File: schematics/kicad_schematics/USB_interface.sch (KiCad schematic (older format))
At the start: 13 parts, among them Q1 NPN, Q2 NPN, U8 USB-TYPEB, U9 USBLC6-2P6

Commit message: added modules do-124ab package
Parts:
- removed Q1, Q2: NPN, -SOT23, symbol NPN
- added Q1, Q2: NPN-SC-59, symbol NPN-SC-59
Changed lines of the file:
@@
-EESchema Schematic File Version 2  date Sun 14 Mar 2010 01:29:31 PM EDT
+EESchema Schematic File Version 2  date Sun 14 Mar 2010 02:53:54 PM EDT
 LIBS:power
 LIBS:device
@@
 Comment4 ""
 $EndDescr
+$Comp
+L NPN-SC-59 Q2
+U 1 1 4B9D3096
+P 5100 4750
+F 0 "Q2" H 5100 4600 50  0000 R CNN
+F 1 "NPN-SC-59" H 5100 4900 50  0000 R CNN
+	1    5100 4750
+	0    -1   -1   0
+$EndComp
+$Comp
+L NPN-SC-59 Q1
+U 1 1 4B9D3085
+P 4750 4050
+F 0 "Q1" H 4750 3900 50  0000 R CNN
+F 1 "NPN-SC-59" H 4750 4200 50  0000 R CNN
+	1    4750 4050
+	0    -1   -1   0
+$EndComp
 Connection ~ 3750 4250
 Wire Wire Line
@@
 $EndComp
 $Comp
-L NPN Q2
-U 1 1 4B7E94E8
-P 5100 4750
-F 0 "Q2" H 5250 4750 50  0000 C CNN
-F 1 "NPN" H 5002 4900 50  0000 C CNN
-F 2 "-SOT23" H 5100 4750 60  0001 C CNN
-F 4 "BC847_BC547" H 5100 4750 60  0001 C CNN "Part"
-	1    5100 4750
-	0    -1   -1   0
-$EndComp
-$Comp
 L GND #PWR058
 U 1 1 4B7E94D3
@@
 $EndComp
 $Comp
-L NPN Q1
-U 1 1 4B7E94BC
-P 4750 4050
-F 0 "Q1" H 4900 4050 50  0000 C CNN
-F 1 "NPN" H 4652 4200 50  0000 C CNN
-F 2 "-SOT23" H 4750 4050 60  0001 C CNN
-F 4 "BC847_BC547" H 4750 4050 60  0001 C CNN "Part"
-	1    4750 4050
-	0    -1   -1   0
-$EndComp
-$Comp

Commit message: made some usb changes
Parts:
- removed U8: USB-TYPEB, mini-usb-b, symbol USB-TYPEB
- added U8: USB-MINI-B-SHELL, symbol USB-MINI-B-SHELL
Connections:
- no-connect marks 0 -> 1
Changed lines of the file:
@@
-EESchema Schematic File Version 2  date Sun 14 Mar 2010 02:53:54 PM EDT
+EESchema Schematic File Version 2  date Sun 14 Mar 2010 03:28:34 PM EDT
 LIBS:power
 LIBS:device
@@
 Comment4 ""
 $EndDescr
+NoConn ~ 3500 3350
+Wire Wire Line
+	3900 3500 3900 4250
+Wire Wire Line
+	3900 3500 3500 3500
+Connection ~ 3750 4250
+Wire Wire Line
+	3900 4250 3500 4250
+Wire Wire Line
+	5950 4500 5950 4350
+Wire Wire Line
+	6600 5100 5100 5100
+Wire Wire Line
+	5100 5100 5100 4950
+Wire Wire Line
+	5300 4650 5500 4650
+Wire Wire Line
+	5500 4800 5500 4400
+Wire Wire Line
+	5500 4400 5400 4400
+Wire Wire Line
+	4650 4400 4900 4400
+Wire Wire Line
+	4100 3950 4550 3950
+Connection ~ 5850 3350
+Wire Wire Line
+	5850 3350 5850 3950
+Wire Wire Line
+	5850 3950 5550 3950
+Connection ~ 5850 2450
+Wire Wire Line
+	6150 2450 5850 2450
+Wire Wire Line
+	7450 3050 6750 3050
+Wire Wire Line
+	6250 3050 5650 3050
+Wire Wire Line
+	5650 3200 5850 3200
+Wire Wire Line
+	4450 3350 4050 3350
+Wire Wire Line
+	4050 3350 4050 3200
+Wire Wire Line
+	4050 3200 3500 3200
+Wire Wire Line
+	4450 3200 4200 3200
+Wire Wire Line
+	3500 4250 3500 4150
+Wire Wire Line
+	3750 4250 3750 4200
+Wire Wire Line
+	3750 3650 3500 3650
+Wire Wire Line
+	3750 3650 3750 3700
+Connection ~ 3500 3650
+Wire Wire Line
+	4450 3050 3500 3050
+Wire Wire Line
+	3500 2900 3700 2900
+Wire Wire Line
+	3700 2900 3700 2850
+Wire Wire Line
+	6250 3350 5650 3350
+Wire Wire Line
+	6750 3350 7450 3350
+Wire Wire Line
+	6150 2850 6150 2950
+Wire Wire Line
+	5850 3200 5850 2400
+Wire Wire Line
+	5050 3950 4950 3950
+Wire Wire Line
+	4100 4300 4100 4400
+Wire Wire Line
+	4100 4400 4150 4400
+Wire Wire Line
+	4750 4250 4750 4650
+Wire Wire Line
+	4750 4650 4900 4650
+Connection ~ 5500 4650
+Wire Wire Line
+	5950 5000 5950 5100
+Connection ~ 5950 5100
+Wire Wire Line
+	3300 2550 3550 2550
+Wire Wire Line
+	3550 2550 3550 2900
+Connection ~ 3550 2900
+Wire Wire Line
+	3650 4250 3650 4350
+Wire Wire Line
+	3500 3650 3500 3750
+$Comp
+L USB-MINI-B-SHELL U8
+U 1 1 4B9D385E
+P 3100 3200
+F 0 "U8" H 3050 3650 60  0000 C CNN
+F 1 "USB-MINI-B-SHELL" H 3250 2600 60  0000 C CNN
+	1    3100 3200
+	-1   0    0    -1
+$EndComp
 $Comp
 L NPN-SC-59 Q2
@@
 	0    -1   -1   0
 $EndComp
-Connection ~ 3750 4250
-Wire Wire Line
-	3900 4250 3500 4250
-Wire Wire Line
-	3900 4250 3900 3350
-Wire Wire Line
-	3900 3350 3500 3350
-Wire Wire Line
-	5950 4500 5950 4350
-Wire Wire Line
-	6600 5100 5100 5100
-Wire Wire Line
-	5100 5100 5100 4950
-Wire Wire Line
-	5300 4650 5500 4650
-Wire Wire Line
-	5500 4800 5500 4400
-Wire Wire Line
-	5500 4400 5400 4400
-Wire Wire Line
-	4650 4400 4900 4400
-Wire Wire Line
-	4100 3950 4550 3950
-Connection ~ 5850 3350
-Wire Wire Line
-	5850 3350 5850 3950
-Wire Wire Line
-	5850 3950 5550 3950
-Connection ~ 5850 2450
-Wire Wire Line
-	6150 2450 5850 2450
-Wire Wire Line
-	7450 3050 6750 3050
-Wire Wire Line
-	6250 3050 5650 3050
-Wire Wire Line
-	5650 3200 5850 3200
-Wire Wire Line
-	4450 3350 4050 3350
-Wire Wire Line
-	4050 3350 4050 3200
-Wire Wire Line
-	4050 3200 3500 3200
-Wire Wire Line
-	4450 3200 4200 3200
-Wire Wire Line
-	3500 3500 3500 3750
-Wire Wire Line
-	3500 4250 3500 4150
-Wire Wire Line
-	3750 4250 3750 4200
-Wire Wire Line
-	3500 3650 3750 3650
-Wire Wire Line
-	3750 3650 3750 3700
-Connection ~ 3500 3650
-Wire Wire Line
-	4450 3050 3500 3050
-Wire Wire Line
-	3500 2900 3700 2900
-Wire Wire Line
-	3700 2900 3700 2850
-Wire Wire Line
-	6250 3350 5650 3350
-Wire Wire Line
-	6750 3350 7450 3350
-Wire Wire Line
-	6150 2850 6150 2950
-Wire Wire Line
-	5850 3200 5850 2400
-Wire Wire Line
-	5050 3950 4950 3950
-Wire Wire Line
-	4100 4300 4100 4400
-Wire Wire Line
-	4100 4400 4150 4400
-Wire Wire Line
-	4750 4250 4750 4650
-Wire Wire Line
-	4750 4650 4900 4650
-Connection ~ 5500 4650
-Wire Wire Line
-	5950 5000 5950 5100
-Connection ~ 5950 5100
-Wire Wire Line
-	3300 2550 3550 2550
-Wire Wire Line
-	3550 2550 3550 2900
-Connection ~ 3550 2900
-Wire Wire Line
-	3650 4250 3650 4350
 $Comp
 L GND #PWR056
@@
 	1    0    0    -1
 $EndComp
-$Comp
-L USB-TYPEB U8
-U 1 1 4B7E9254
-P 3100 3200
-F 0 "U8" H 3050 3650 60  0000 C CNN
-F 1 "USB-TYPEB" H 3300 2600 60  0000 C CNN
-F 2 "mini-usb-b" H 3100 3200 60  0001 C CNN
-	1    3100 3200
-	-1   0    0    -1
-$EndComp
 $EndSCHEMATC

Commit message: modified pinout on em406, update schematic, and modified pinout on S08 and SSOT6
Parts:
- Q1, Q2: footprint (none) -> -SOT23
- U8: footprint (none) -> mini-usb-b-shell
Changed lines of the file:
@@
-EESchema Schematic File Version 2  date Sun 14 Mar 2010 03:28:34 PM EDT
+EESchema Schematic File Version 2  date Sun 14 Mar 2010 03:55:01 PM EDT
 LIBS:power
 LIBS:device
@@
 F 0 "U8" H 3050 3650 60  0000 C CNN
 F 1 "USB-MINI-B-SHELL" H 3250 2600 60  0000 C CNN
+F 2 "mini-usb-b-shell" H 3100 3200 60  0001 C CNN
 	1    3100 3200
 	-1   0    0    -1
@@
 F 0 "Q2" H 5100 4600 50  0000 R CNN
 F 1 "NPN-SC-59" H 5100 4900 50  0000 R CNN
+F 2 "-SOT23" H 5100 4750 60  0001 C CNN
 	1    5100 4750
 	0    -1   -1   0
@@
 F 0 "Q1" H 4750 3900 50  0000 R CNN
 F 1 "NPN-SC-59" H 4750 4200 50  0000 R CNN
+F 2 "-SOT23" H 4750 4050 60  0001 C CNN
 	1    4750 4050
 	0    -1   -1   0
 $EndComp
 $Comp
-L GND #PWR056
+L GND #PWR055
 U 1 1 4B9843F1
 P 3650 4350
-F 0 "#PWR056" H 3650 4350 30  0001 C CNN
+F 0 "#PWR055" H 3650 4350 30  0001 C CNN
 F 1 "GND" H 3650 4280 30  0001 C CNN
 	1    3650 4350
@@
 $EndComp
 $Comp
-L 3V3 #PWR057
+L 3V3 #PWR056
 U 1 1 4B7E9511
 P 4100 4300
-F 0 "#PWR057" H 4100 4400 40  0001 C CNN
+F 0 "#PWR056" H 4100 4400 40  0001 C CNN
 F 1 "U5V" H 4100 4449 40  0000 C CNN
 	1    4100 4300
@@
 $EndComp
 $Comp
-L GND #PWR058
+L GND #PWR057
 U 1 1 4B7E94D3
 P 6150 2950
-F 0 "#PWR058" H 6150 2950 30  0001 C CNN
+F 0 "#PWR057" H 6150 2950 30  0001 C CNN
 F 1 "GND" H 6150 2880 30  0001 C CNN
 	1    6150 2950
@@
 $EndComp
 $Comp
-L 3V3 #PWR059
+L 3V3 #PWR058
 U 1 1 4B7E945B
 P 5850 2400
-F 0 "#PWR059" H 5850 2500 40  0001 C CNN
+F 0 "#PWR058" H 5850 2500 40  0001 C CNN
 F 1 "U5V" H 5850 2549 40  0000 C CNN
 	1    5850 2400
@@
 $EndComp
 $Comp
-L GND #PWR060
+L GND #PWR059
 U 1 1 4B7E9432
 P 5500 4800
-F 0 "#PWR060" H 5500 4800 30  0001 C CNN
+F 0 "#PWR059" H 5500 4800 30  0001 C CNN
 F 1 "GND" H 5500 4730 30  0001 C CNN
 	1    5500 4800
@@
 $EndComp
 $Comp
-L 3V3 #PWR061
+L 3V3 #PWR060
 U 1 1 4B7E93C0
 P 3700 2850
-F 0 "#PWR061" H 3700 2950 40  0001 C CNN
+F 0 "#PWR060" H 3700 2950 40  0001 C CNN
 F 1 "U5V" H 3700 2999 40  0000 C CNN
 	1    3700 2850
@@
 $EndComp
 $Comp
-L GND #PWR062
+L GND #PWR061
 U 1 1 4B7E92CC
 P 4200 3200
-F 0 "#PWR062" H 4200 3200 30  0001 C CNN
+F 0 "#PWR061" H 4200 3200 30  0001 C CNN
 F 1 "GND" H 4200 3130 30  0001 C CNN
 	1    4200 3200

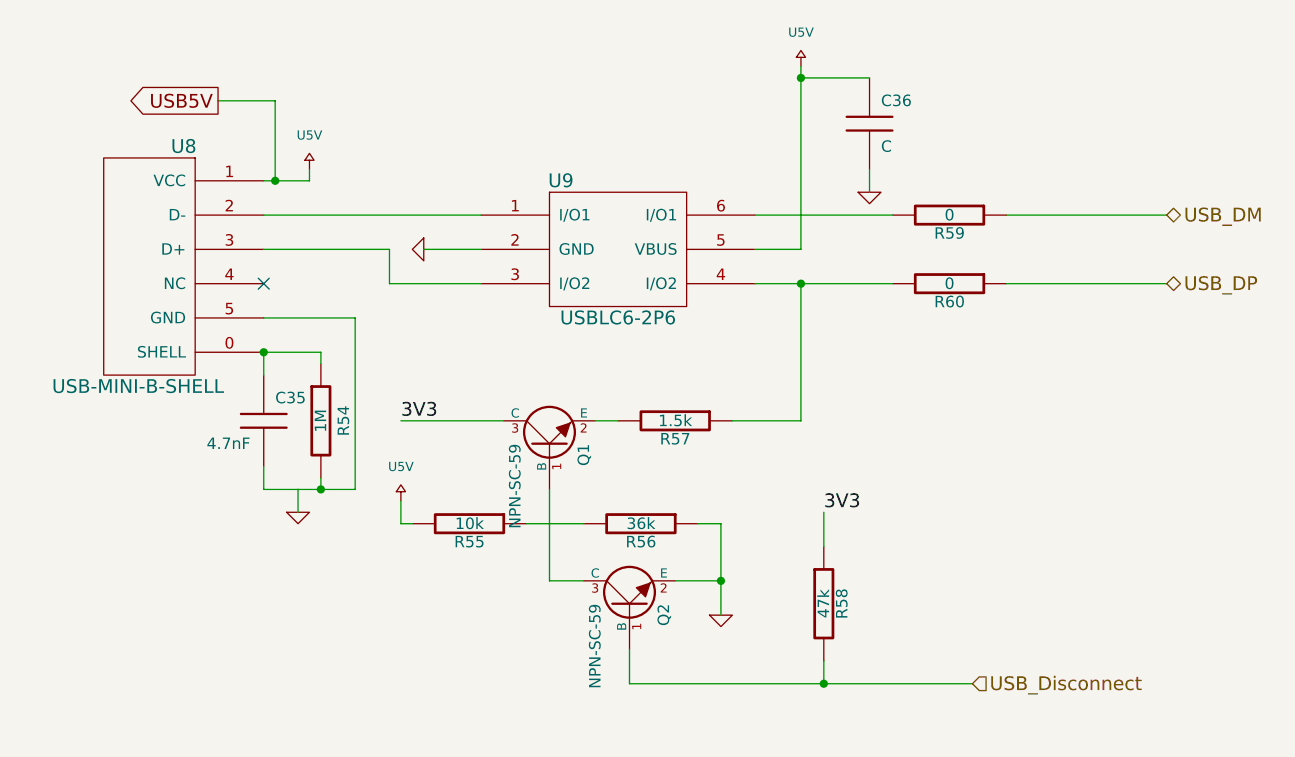
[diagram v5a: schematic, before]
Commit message: Modified power libraries. Now using custom power.lib. This is important Removed outdated crystal libaries Changed some caps to 0603 mounts started PCB layout
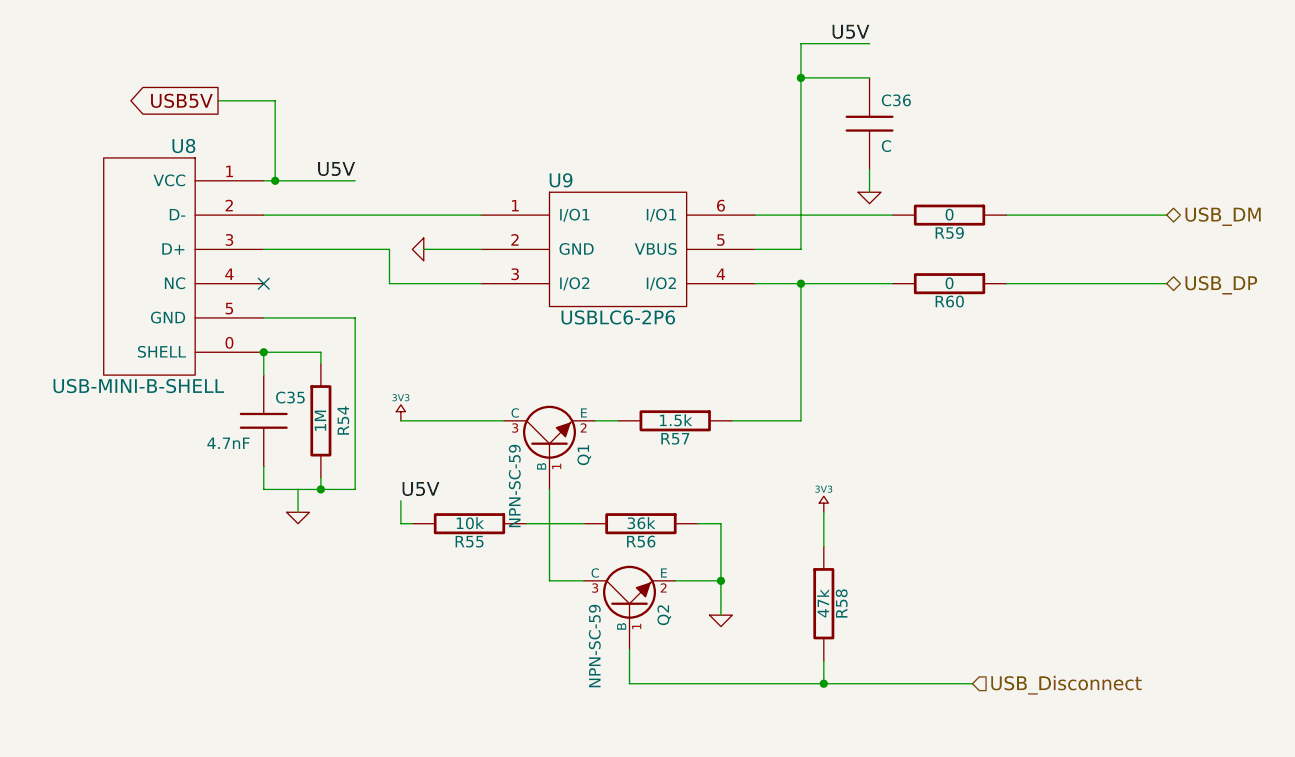
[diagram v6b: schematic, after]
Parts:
- C35, C36, R54, R55, R56, R57, R58, R59, R60: footprint SM0805 -> SM0805-CUSTOM
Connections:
- net 3V3: no longer C36.1, R55.2, U8.1 (VCC), U9.5 (VBUS)
- new net USB5V: C36.1, R55.2, U8.1 (VCC), U9.5 (VBUS)
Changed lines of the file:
@@
-EESchema Schematic File Version 2  date Mon 15 Mar 2010 09:49:52 PM EDT
+EESchema Schematic File Version 2  date Tue 16 Mar 2010 05:07:11 PM EDT
 LIBS:power
 LIBS:device
@@
 Comment4 ""
 $EndDescr
+$Comp
+L GND #PWR073
+U 1 1 4B9FDA7B
+P 4200 3200
+F 0 "#PWR073" H 4200 3200 30  0001 C CNN
+F 1 "GND" H 4200 3130 30  0001 C CNN
+	1    4200 3200
+	0    1    1    0
+$EndComp
+$Comp
+L GND #PWR074
+U 1 1 4B9FDA6F
+P 6150 2950
+F 0 "#PWR074" H 6150 2950 30  0001 C CNN
+F 1 "GND" H 6150 2880 30  0001 C CNN
+	1    6150 2950
+	1    0    0    -1
+$EndComp
+$Comp
+L 3V3 #PWR075
+U 1 1 4B9FDA6B
+P 5950 4350
+F 0 "#PWR075" H 5950 4480 20  0001 C CNN
+F 1 "3V3" H 5950 4450 30  0000 C CNN
+	1    5950 4350
+	1    0    0    -1
+$EndComp
+$Comp
+L GND #PWR076
+U 1 1 4B9FDA67
+P 5500 4800
+F 0 "#PWR076" H 5500 4800 30  0001 C CNN
+F 1 "GND" H 5500 4730 30  0001 C CNN
+	1    5500 4800
+	1    0    0    -1
+$EndComp
+$Comp
+L 3V3 #PWR077
+U 1 1 4B9FDA63
+P 4100 3950
+F 0 "#PWR077" H 4100 4080 20  0001 C CNN
+F 1 "3V3" H 4100 4050 30  0000 C CNN
+	1    4100 3950
+	1    0    0    -1
+$EndComp
+$Comp
+L GND #PWR078
+U 1 1 4B9FDA5F
+P 3650 4350
+F 0 "#PWR078" H 3650 4350 30  0001 C CNN
+F 1 "GND" H 3650 4280 30  0001 C CNN
+	1    3650 4350
+	1    0    0    -1
+$EndComp
+Text Label 4100 4300 0    60   ~ 0
+U5V
+Text Label 6150 2300 2    60   ~ 0
+U5V
+Connection ~ 5850 2450
+Wire Wire Line
+	6150 2300 5850 2300
+Wire Wire Line
+	5850 2300 5850 3200
+Wire Wire Line
+	3500 3750 3500 3650
+Wire Wire Line
+	3650 4250 3650 4350
+Connection ~ 3550 2900
+Wire Wire Line
+	3550 2900 3550 2550
+Wire Wire Line
+	3550 2550 3300 2550
+Connection ~ 5950 5100
+Wire Wire Line
+	5950 5000 5950 5100
+Connection ~ 5500 4650
+Wire Wire Line
+	4900 4650 4750 4650
+Wire Wire Line
+	4750 4650 4750 4250
+Wire Wire Line
+	4150 4400 4100 4400
+Wire Wire Line
+	4100 4400 4100 4300
+Wire Wire Line
+	5050 3950 4950 3950
+Wire Wire Line
+	6150 2850 6150 2950
+Wire Wire Line
+	6750 3350 7450 3350
+Wire Wire Line
+	5650 3350 6250 3350
+Wire Wire Line
+	3900 2900 3500 2900
+Wire Wire Line
+	4450 3050 3500 3050
+Connection ~ 3500 3650
+Wire Wire Line
+	3750 3700 3750 3650
+Wire Wire Line
+	3750 3650 3500 3650
+Wire Wire Line
+	3750 4200 3750 4250
+Wire Wire Line
+	3500 4150 3500 4250
+Wire Wire Line
+	4450 3200 4200 3200
+Wire Wire Line
+	3500 3200 4050 3200
+Wire Wire Line
+	4050 3200 4050 3350
+Wire Wire Line
+	4050 3350 4450 3350
+Wire Wire Line
+	5850 3200 5650 3200
+Wire Wire Line
+	6250 3050 5650 3050
+Wire Wire Line
+	7450 3050 6750 3050
+Wire Wire Line
+	5850 2450 6150 2450
+Wire Wire Line
+	5550 3950 5850 3950
+Wire Wire Line
+	5850 3950 5850 3350
+Connection ~ 5850 3350
+Wire Wire Line
+	4100 3950 4550 3950
+Wire Wire Line
+	4650 4400 4900 4400
+Wire Wire Line
+	5400 4400 5500 4400
+Wire Wire Line
+	5500 4400 5500 4800
+Wire Wire Line
+	5300 4650 5500 4650
+Wire Wire Line
+	5100 4950 5100 5100
+Wire Wire Line
+	5100 5100 6600 5100
+Wire Wire Line
+	5950 4500 5950 4350
+Wire Wire Line
+	3500 4250 3900 4250
+Connection ~ 3750 4250
+Wire Wire Line
+	3500 3500 3900 3500
+Wire Wire Line
+	3900 3500 3900 4250
+Text Label 3900 2900 2    60   ~ 0
+U5V
 NoConn ~ 3500 3350
-Wire Wire Line
-	3900 3500 3900 4250
-Wire Wire Line
-	3900 3500 3500 3500
-Connection ~ 3750 4250
-Wire Wire Line
-	3900 4250 3500 4250
-Wire Wire Line
-	5950 4500 5950 4350
-Wire Wire Line
-	6600 5100 5100 5100
-Wire Wire Line
-	5100 5100 5100 4950
-Wire Wire Line
-	5300 4650 5500 4650
-Wire Wire Line
-	5500 4800 5500 4400
-Wire Wire Line
-	5500 4400 5400 4400
-Wire Wire Line
-	4650 4400 4900 4400
-Wire Wire Line
-	4100 3950 4550 3950
-Connection ~ 5850 3350
-Wire Wire Line
-	5850 3350 5850 3950
-Wire Wire Line
-	5850 3950 5550 3950
-Connection ~ 5850 2450
-Wire Wire Line
-	6150 2450 5850 2450
-Wire Wire Line
-	7450 3050 6750 3050
-Wire Wire Line
-	6250 3050 5650 3050
-Wire Wire Line
-	5650 3200 5850 3200
-Wire Wire Line
-	4450 3350 4050 3350
-Wire Wire Line
-	4050 3350 4050 3200
-Wire Wire Line
-	4050 3200 3500 3200
-Wire Wire Line
-	4450 3200 4200 3200
-Wire Wire Line
-	3500 4250 3500 4150
-Wire Wire Line
-	3750 4250 3750 4200
-Wire Wire Line
-	3750 3650 3500 3650
-Wire Wire Line
-	3750 3650 3750 3700
-Connection ~ 3500 3650
-Wire Wire Line
-	4450 3050 3500 3050
-Wire Wire Line
-	3500 2900 3700 2900
-Wire Wire Line
-	3700 2900 3700 2850
-Wire Wire Line
-	6250 3350 5650 3350
-Wire Wire Line
-	6750 3350 7450 3350
-Wire Wire Line
-	6150 2850 6150 2950
-Wire Wire Line
-	5850 3200 5850 2400
-Wire Wire Line
-	5050 3950 4950 3950
-Wire Wire Line
-	4100 4300 4100 4400
-Wire Wire Line
-	4100 4400 4150 4400
-Wire Wire Line
-	4750 4250 4750 4650
-Wire Wire Line
-	4750 4650 4900 4650
-Connection ~ 5500 4650
-Wire Wire Line
-	5950 5000 5950 5100
-Connection ~ 5950 5100
-Wire Wire Line
-	3300 2550 3550 2550
-Wire Wire Line
-	3550 2550 3550 2900
-Connection ~ 3550 2900
-Wire Wire Line
-	3650 4250 3650 4350
-Wire Wire Line
-	3500 3650 3500 3750
 $Comp
 L USB-MINI-B-SHELL U8
@@
 	0    -1   -1   0
 $EndComp
-$Comp
-L GND #PWR67
-U 1 1 4B9843F1
-P 3650 4350
-F 0 "#PWR67" H 3650 4350 30  0001 C CNN
-F 1 "GND" H 3650 4280 30  0001 C CNN
-	1    3650 4350
-	1    0    0    -1
-$EndComp
 Text GLabel 3300 2550 0    60   Output ~ 0
 USB5V
@@
 Text HLabel 6600 5100 2    60   Input ~ 0
 USB_Disconnect
-Text Label 5950 4350 0    60   ~ 0
-3V3
-Text Label 4100 3950 0    60   ~ 0
-3V3
 $Comp
 L R R58
@@
 F 0 "R58" V 6030 4750 50  0000 C CNN
 F 1 "47k" V 5950 4750 50  0000 C CNN
-F 2 "SM0805" H 5950 4750 60  0001 C CNN
+F 2 "SM0805-CUSTOM" H 5950 4750 60  0001 C CNN
 	1    5950 4750
 	1    0    0    -1
@@
 F 0 "R55" V 4480 4400 50  0000 C CNN
 F 1 "10k" V 4400 4400 50  0000 C CNN
-F 2 "SM0805" H 4400 4400 60  0001 C CNN
+F 2 "SM0805-CUSTOM" H 4400 4400 60  0001 C CNN
 	1    4400 4400
 	0    1    1    0
@@
 F 0 "R56" V 5230 4400 50  0000 C CNN
 F 1 "36k" V 5150 4400 50  0000 C CNN
-F 2 "SM0805" H 5150 4400 60  0001 C CNN
+F 2 "SM0805-CUSTOM" H 5150 4400 60  0001 C CNN
 	1    5150 4400
 	0    1    1    0
@@
 F 0 "R57" V 5380 3950 50  0000 C CNN
 F 1 "1.5k" V 5300 3950 50  0000 C CNN
-F 2 "SM0805" H 5300 3950 60  0001 C CNN
+F 2 "SM0805-CUSTOM" H 5300 3950 60  0001 C CNN
 	1    5300 3950
 	0    1    1    0
-$EndComp
-$Comp
-L 3V3 #PWR69
-U 1 1 4B7E9511
-P 4100 4300
-F 0 "#PWR69" H 4100 4400 40  0001 C CNN
-F 1 "U5V" H 4100 4449 40  0000 C CNN
-	1    4100 4300
-	1    0    0    -1
-$EndComp
-$Comp
-L GND #PWR73
-U 1 1 4B7E94D3
-P 6150 2950
-F 0 "#PWR73" H 6150 2950 30  0001 C CNN
-F 1 "GND" H 6150 2880 30  0001 C CNN
-	1    6150 2950
-	1    0    0    -1
 $EndComp
 $Comp
@@
 F 0 "C36" H 6200 2750 50  0000 L CNN
 F 1 "C" H 6200 2550 50  0000 L CNN
-F 2 "SM0805" H 6150 2650 60  0001 C CNN
+F 2 "SM0805-CUSTOM" H 6150 2650 60  0001 C CNN
 	1    6150 2650
 	1    0    0    -1
@@
 F 0 "R60" V 6580 3350 50  0000 C CNN
 F 1 "0" V 6500 3350 50  0000 C CNN
-F 2 "SM0805" H 6500 3350 60  0001 C CNN
+F 2 "SM0805-CUSTOM" H 6500 3350 60  0001 C CNN
 	1    6500 3350
 	0    1    1    0
@@
 F 0 "R59" V 6580 3050 50  0000 C CNN
 F 1 "0" V 6500 3050 50  0000 C CNN
-F 2 "SM0805" H 6500 3050 60  0001 C CNN
+F 2 "SM0805-CUSTOM" H 6500 3050 60  0001 C CNN
 	1    6500 3050
 	0    1    1    0
-$EndComp
-$Comp
-L 3V3 #PWR72
-U 1 1 4B7E945B
-P 5850 2400
-F 0 "#PWR72" H 5850 2500 40  0001 C CNN
-F 1 "U5V" H 5850 2549 40  0000 C CNN
-	1    5850 2400
-	1    0    0    -1
-$EndComp
-$Comp
-L GND #PWR71
-U 1 1 4B7E9432
-P 5500 4800
-F 0 "#PWR71" H 5500 4800 30  0001 C CNN
-F 1 "GND" H 5500 4730 30  0001 C CNN
-	1    5500 4800
-	1    0    0    -1
 $EndComp
 $Comp
@@
 F 0 "R54" V 3850 3950 50  0000 C CNN
 F 1 "1M" V 3750 3950 50  0000 C CNN
-F 2 "SM0805" H 3750 3950 60  0001 C CNN
+F 2 "SM0805-CUSTOM" H 3750 3950 60  0001 C CNN
 	1    3750 3950
 	1    0    0    -1
@@
 F 0 "C35" H 3550 4050 50  0000 L CNN
 F 1 "4.7nF" H 3250 3850 50  0000 L CNN
-F 2 "SM0805" H 3500 3950 60  0001 C CNN
+F 2 "SM0805-CUSTOM" H 3500 3950 60  0001 C CNN
 	1    3500 3950
 	1    0    0    -1
 $EndComp
 $Comp
-L 3V3 #PWR68
-U 1 1 4B7E93C0
-P 3700 2850
-F 0 "#PWR68" H 3700 2950 40  0001 C CNN
-F 1 "U5V" H 3700 2999 40  0000 C CNN
-	1    3700 2850
-	1    0    0    -1
-$EndComp
-$Comp
-L GND #PWR70
-U 1 1 4B7E92CC
-P 4200 3200
-F 0 "#PWR70" H 4200 3200 30  0001 C CNN
-F 1 "GND" H 4200 3130 30  0001 C CNN
-	1    4200 3200
-	0    1    1    0
-$EndComp
-$Comp
